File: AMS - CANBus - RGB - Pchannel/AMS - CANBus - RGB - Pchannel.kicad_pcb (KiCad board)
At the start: 2 copper layers, 72.9 x 71.1 mm, 51 parts, among them J1 Power_And_CAN, J2 Screw_Terminal_01x05, J3 TTL_Programmer, J4 ICSP, J5 Conn_01x02, Q1 IRF9Z34NPBF, Q10 2N7002, Q2 IRF510, Q3 IRF510, Q4 IRF510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

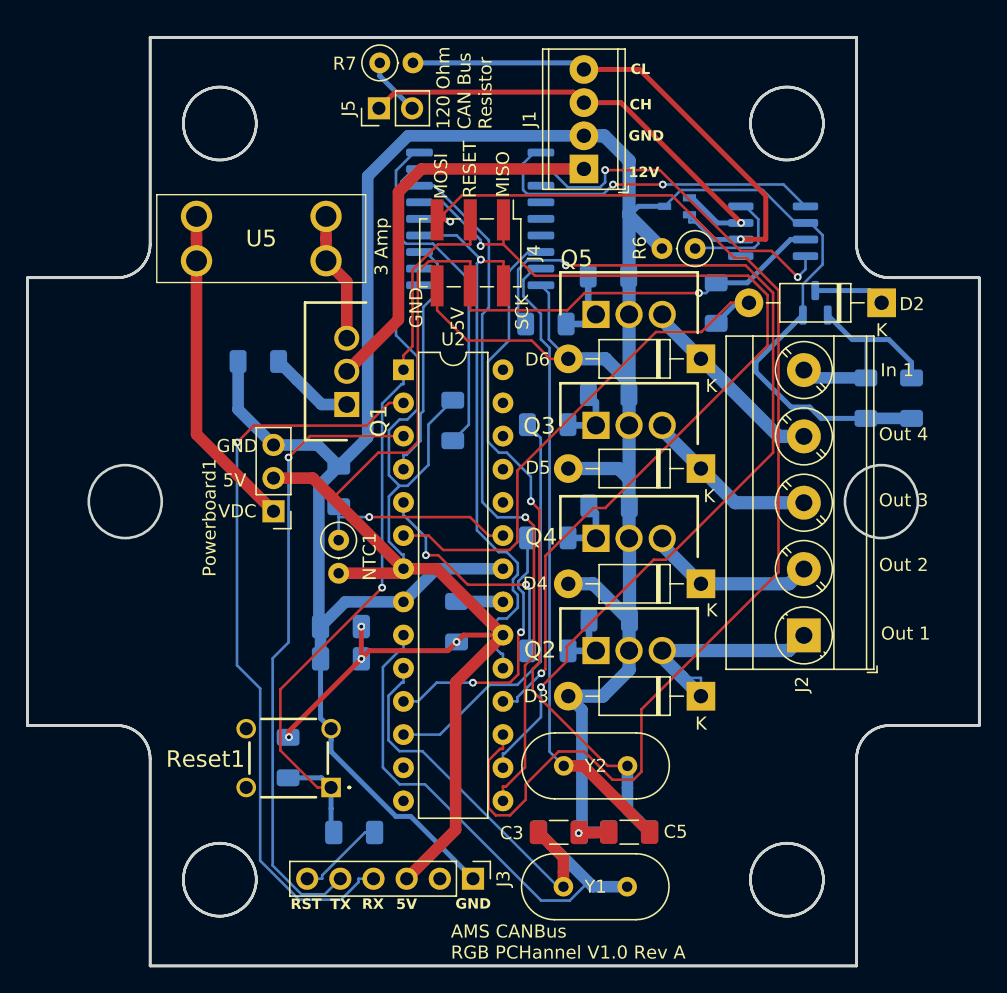
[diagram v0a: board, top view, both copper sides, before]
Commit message: clean up to avoid serpac case mounting bosses.
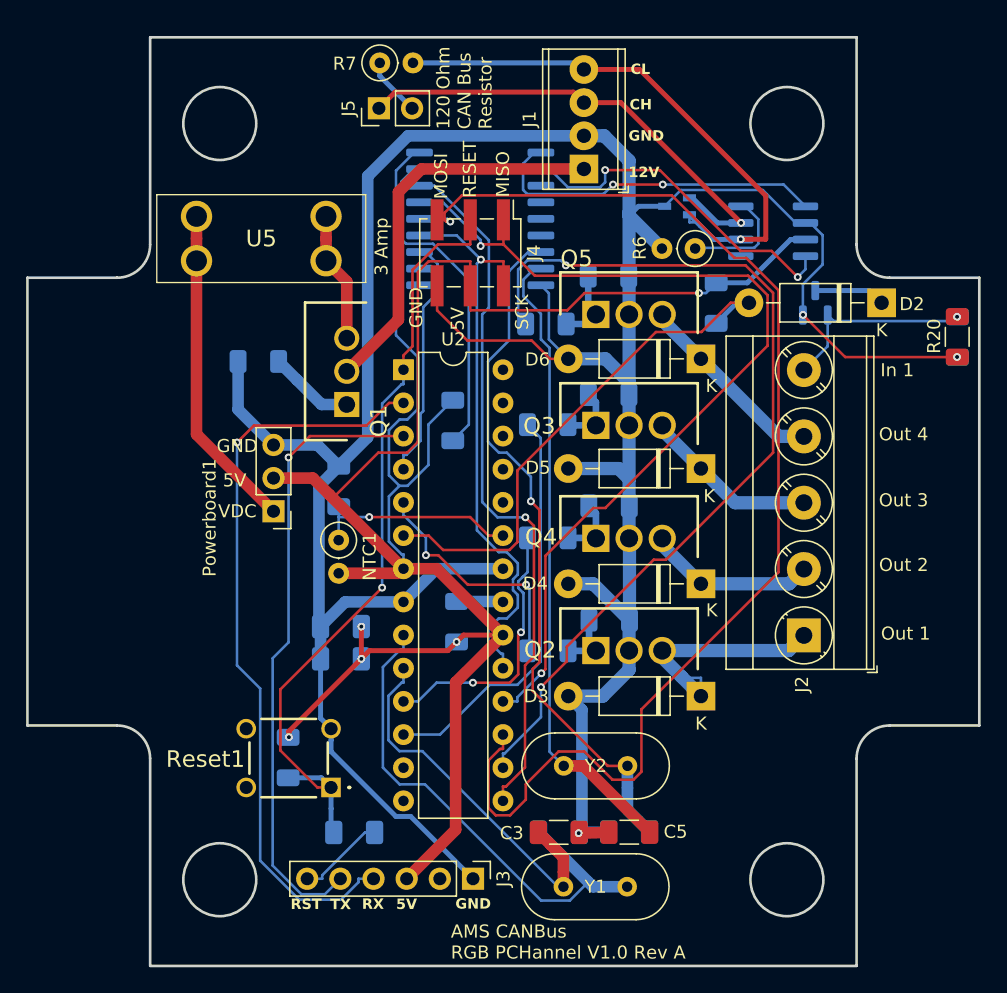
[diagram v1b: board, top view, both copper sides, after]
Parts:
- R20: moved to F.Cu
- moved R20 8.43 mm to (183.3, 79.2)
- moved C8 5.85 mm to (183.4, 79.3)
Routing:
- net GND: track 254.0 -> 247.9 mm, vias 1 -> 3
- net Net-(J2-Pin_5): track 16.2 -> 15.2 mm, vias 0 -> 1
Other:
- outline, holes or cut-outs redrawn
